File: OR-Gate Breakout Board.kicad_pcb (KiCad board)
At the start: 2 copper layers, 5.5 x 5.4 mm, 8 parts, among them U5 74LVC1G332GW,125

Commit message: Updated design to be a little more usable. Still need to consider resistors and stuff. Do not use this version. WIP
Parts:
- added ?: , , F.Cu at (155.2, 97.8)
- moved ? 8.84 mm to (142.2, 99.1)
- moved ? 8.67 mm to (142.2, 92.7)
- moved ? 8.61 mm to (142.2, 95.8)
- moved C1 5.19 mm to (147.9, 99.1)
- moved U5 5.08 mm to (147.9, 95.5)
- moved ? 2.44 mm to (154.4, 99.3)
- moved ? 1.96 mm to (153.7, 92.7)
- moved ? 1.52 mm to (153.7, 95.8)
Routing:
- net GND: track 4.08 -> 8.85 mm
- net VCC: track 4.46 -> 8.88 mm
- net OUT: track 1.25 -> 5.61 mm
- net B: track 1.17 -> 5.35 mm
- net C: track 1.25 -> 5.10 mm
- net A: track 1.23 -> 5.02 mm
- removed copper zone on B.Cu, net GND
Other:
- board size 5.5 x 5.4 mm -> 17 x 9.1 mm
- board text added: "A"
- board text added: "B"
- board text added: "C"
- board text added: "GND"
- board text added: "OUT"
- board text added: "VCC"

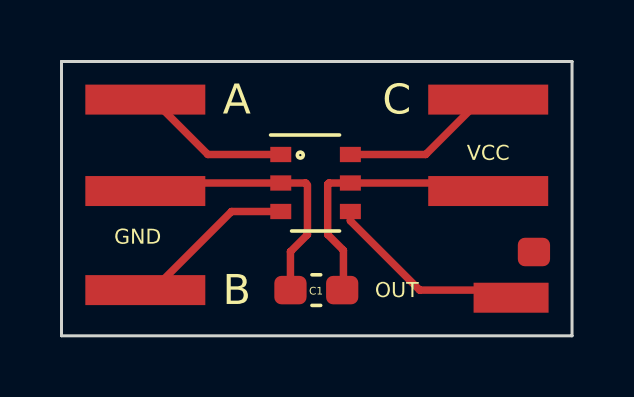
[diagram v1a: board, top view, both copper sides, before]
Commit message: Alpha Prototype for OR Gate Breakout.
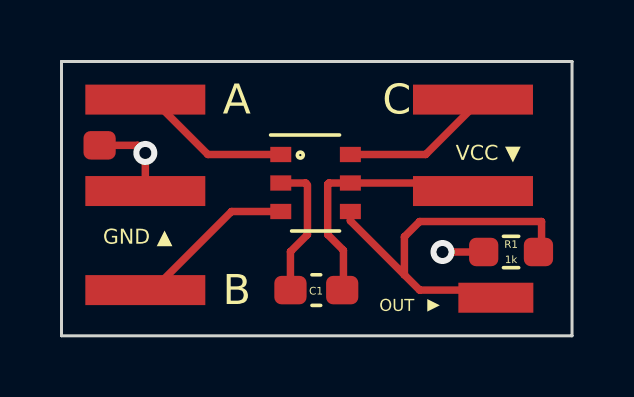
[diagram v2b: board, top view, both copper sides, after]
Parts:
- added 1k: 1k, Resistor_SMD:R_0603_1608Metric_Pad0.98x0.95mm_HandSolder, F.Cu at (154.4, 97.8)
- moved ? 14.9 mm to (140.7, 94.2)
- moved ? 0.51 mm to (153.2, 95.8)
- moved ? 0.51 mm to (153.9, 99.3)
- moved ? 0.51 mm to (153.2, 92.7)
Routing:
- net OUT: track 5.61 -> 12.7 mm
- net GND: track 8.85 -> 9.13 mm, vias 0 -> 2
- added copper zone on B.Cu, net GND
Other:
- board text added: "GND ▲"
- board text added: "R1"
- board text added: "VCC ▼"
- board text added: "▲"
- board text removed: "GND"
- board text removed: "VCC"
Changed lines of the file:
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@@
   )
   (footprint "" (layer "F.Cu")
-    (at 153.67 95.758)
+    (at 153.162 95.758)
     (fp_text reference "" (at 0 0) (layer "F.SilkS")
       (effects (font (size 1.27 1.27) (thickness 0.15)))
@@
   )
   (footprint "" (layer "F.Cu")
-    (at 154.432 99.314)
+    (at 153.924 99.314)
     (fp_text reference "" (at 0 0) (layer "F.SilkS")
       (effects (font (size 1.27 1.27) (thickness 0.15)))
@@
       (net 2 "GND"))
   )
-  (footprint "" (layer "F.Cu")
-    (at 155.194 97.79)
-    (fp_text reference "" (at 0 0) (layer "F.SilkS")
-      (effects (font (size 1.27 1.27) (thickness 0.15)))
-    )
-    (fp_text value "" (at 0 0) (layer "F.SilkS")
-      (effects (font (size 1.27 1.27) (thickness 0.15)))
-    )
-    (pad "4" smd roundrect locked (at 0 0) (size 1.075 0.95) (layers "F.Cu" "F.Paste" "F.Mask") (roundrect_rratio 0.25)
+  (footprint "Resistor_SMD:R_0603_1608Metric_Pad0.98x0.95mm_HandSolder" (layer "F.Cu")
+    (at 154.432 97.79)
+    (descr "Resistor SMD 0603 (1608 Metric), square (rectangular) end terminal, IPC_7351 nominal with elongated pad for handsoldering. (Body size source: IPC-SM-782 page 72, https://www.pcb-3d.com/wordpress/wp-content/uploads/ipc-sm-782a_amendment_1_and_2.pdf), generated with kicad-footprint-generator")
+    (tags "resistor handsolder")
+    (attr smd)
+    (fp_text reference "1k" (at 0 0.254) (layer "F.SilkS")
+      (effects (font (size 0.25 0.25) (thickness 0.0625)))
+    )
+    (fp_text value "1k" (at 0 1.43) (layer "F.Fab")
+      (effects (font (size 1 1) (thickness 0.15)))
+    )
+    (fp_text user "${REFERENCE}" (at 0 0) (layer "F.Fab")
+      (effects (font (size 0.4 0.4) (thickness 0.06)))
+    )
+    (fp_line (start -0.254724 0.5225) (end 0.254724 0.5225) (layer "F.SilkS") (width 0.12))
+    (fp_line (start -0.254724 -0.5225) (end 0.254724 -0.5225) (layer "F.SilkS") (width 0.12))
+    (fp_line (start -1.65 -0.73) (end 1.65 -0.73) (layer "F.CrtYd") (width 0.05))
+    (fp_line (start 1.65 -0.73) (end 1.65 0.73) (layer "F.CrtYd") (width 0.05))
+    (fp_line (start -1.65 0.73) (end -1.65 -0.73) (layer "F.CrtYd") (width 0.05))
+    (fp_line (start 1.65 0.73) (end -1.65 0.73) (layer "F.CrtYd") (width 0.05))
+    (fp_line (start 0.8 -0.4125) (end 0.8 0.4125) (layer "F.Fab") (width 0.1))
+    (fp_line (start 0.8 0.4125) (end -0.8 0.4125) (layer "F.Fab") (width 0.1))
+    (fp_line (start -0.8 -0.4125) (end 0.8 -0.4125) (layer "F.Fab") (width 0.1))
+    (fp_line (start -0.8 0.4125) (end -0.8 -0.4125) (layer "F.Fab") (width 0.1))
+    (pad "7" smd roundrect (at -0.9125 0) (size 0.975 0.95) (layers "F.Cu" "F.Paste" "F.Mask") (roundrect_rratio 0.25)
+      (net 2 "GND"))
+    (pad "8" smd roundrect (at 0.9125 0) (size 0.975 0.95) (layers "F.Cu" "F.Paste" "F.Mask") (roundrect_rratio 0.25)
       (net 4 "OUT"))
+    (model "${KICAD6_3DMODEL_DIR}/Resistor_SMD.3dshapes/R_0603_1608Metric.wrl"
+      (offset (xyz 0 0 0))
+      (scale (xyz 1 1 1))
+      (rotate (xyz 0 0 0))
+    )
   )
   (footprint "" (layer "F.Cu")
@@
   )
   (footprint "" (layer "F.Cu")
-    (at 153.67 92.71)
+    (at 140.716 94.234)
+    (fp_text reference "" (at 0 0) (layer "F.SilkS")
+      (effects (font (size 1.27 1.27) (thickness 0.15)))
+    )
+    (fp_text value "" (at 0 0) (layer "F.SilkS")
+      (effects (font (size 1.27 1.27) (thickness 0.15)))
+    )
+    (pad "1" smd roundrect (at 0 0) (size 1.075 0.95) (layers "F.Cu" "F.Paste" "F.Mask") (roundrect_rratio 0.25)
+      (net 2 "GND"))
+  )
+  (footprint "" (layer "F.Cu")
+    (at 153.162 92.71)
     (fp_text reference "" (at 0 0) (layer "F.SilkS")
       (effects (font (size 1.27 1.27) (thickness 0.15)))
@@
   )
   (gr_rect (start 139.446 91.44) (end 156.464 100.584) (layer "Edge.Cuts") (width 0.1) (fill none))
-  (gr_text "GND" (at 141.986 97.282) (layer "F.SilkS")
+  (gr_text "GND ▲" (at 141.986 97.282) (layer "F.SilkS")
     (effects (font (size 0.5 0.5) (thickness 0.125)))
   )
@@
     (effects (font (size 1 1) (thickness 0.15)))
   )
-  (gr_text "VCC" (at 153.67 94.488) (layer "F.SilkS")
+  (gr_text "VCC ▼" (at 153.67 94.488) (layer "F.SilkS")
     (effects (font (size 0.5 0.5) (thickness 0.125)))
+  )
+  (gr_text "▲" (at 151.892 99.568 -90) (layer "F.SilkS")
+    (effects (font (size 0.4 0.4) (thickness 0.1)))
+  )
+  (gr_text "R1" (at 154.432 97.536) (layer "F.SilkS")
+    (effects (font (size 0.25 0.25) (thickness 0.0625)))
   )
   (gr_text "B" (at 145.288 99.06) (layer "F.SilkS")
     (effects (font (size 1 1) (thickness 0.15)))
   )
-  (gr_text "OUT" (at 150.622 99.06) (layer "F.SilkS")
-    (effects (font (size 0.5 0.5) (thickness 0.125)))
+  (gr_text "OUT" (at 150.622 99.568) (layer "F.SilkS")
+    (effects (font (size 0.4 0.4) (thickness 0.1)))
   )
   (gr_text "C" (at 150.622 92.71) (layer "F.SilkS")
@@
   (segment (start 142.494 92.71) (end 144.324 94.54) (width 0.25) (layer "F.Cu") (net 1))
   (segment (start 144.324 94.54) (end 146.755 94.54) (width 0.25) (layer "F.Cu") (net 1))
+  (segment (start 152.146 97.79) (end 153.5195 97.79) (width 0.25) (layer "F.Cu") (net 2))
   (segment (start 146.91 95.49) (end 146.89 95.51) (width 0.25) (layer "F.Cu") (net 2))
   (segment (start 147.0775 97.7785) (end 147.0775 99.06) (width 0.25) (layer "F.Cu") (net 2))
   (segment (start 147.645 95.55) (end 147.645 97.211) (width 0.25) (layer "F.Cu") (net 2))
   (segment (start 147.585 95.49) (end 146.91 95.49) (width 0.25) (layer "F.Cu") (net 2))
+  (segment (start 140.716 94.234) (end 141.986 94.234) (width 0.25) (layer "F.Cu") (net 2))
+  (segment (start 141.986 94.234) (end 142.24 94.488) (width 0.25) (layer "F.Cu") (net 2))
   (segment (start 147.605 95.51) (end 147.585 95.49) (width 0.25) (layer "F.Cu") (net 2))
   (segment (start 142.494 95.758) (end 142.762 95.49) (width 0.25) (layer "F.Cu") (net 2))
   (segment (start 147.645 97.211) (end 147.0775 97.7785) (width 0.25) (layer "F.Cu") (net 2))
-  (segment (start 142.762 95.49) (end 146.755 95.49) (width 0.25) (layer "F.Cu") (net 2))
+  (segment (start 142.24 95.758) (end 142.24 94.488) (width 0.25) (layer "F.Cu") (net 2))
+  (via (at 142.24 94.488) (size 0.8) (drill 0.4) (layers "F.Cu" "B.Cu") (free) (net 2))
+  (via (at 152.146 97.79) (size 0.8) (drill 0.4) (layers "F.Cu" "B.Cu") (net 2))
   (segment (start 145.114 96.44) (end 146.755 96.44) (width 0.25) (layer "F.Cu") (net 3))
   (segment (start 142.494 99.06) (end 145.114 96.44) (width 0.25) (layer "F.Cu") (net 3))
+  (segment (start 150.876 98.552) (end 150.876 97.282) (width 0.25) (layer "F.Cu") (net 4))
+  (segment (start 150.876 98.552) (end 151.384 99.06) (width 0.25) (layer "F.Cu") (net 4))
+  (segment (start 150.876 97.282) (end 151.384 96.774) (width 0.25) (layer "F.Cu") (net 4))
+  (segment (start 155.448 96.774) (end 155.448 97.6865) (width 0.25) (layer "F.Cu") (net 4))
+  (segment (start 155.448 97.6865) (end 155.3445 97.79) (width 0.25) (layer "F.Cu") (net 4))
+  (segment (start 151.384 96.774) (end 155.448 96.774) (width 0.25) (layer "F.Cu") (net 4))
   (segment (start 151.384 99.06) (end 153.416 99.06) (width 0.25) (layer "F.Cu") (net 4))
-  (segment (start 149.075 96.751) (end 151.384 99.06) (width 0.25) (layer "F.Cu") (net 4))
+  (segment (start 149.075 96.751) (end 150.876 98.552) (width 0.25) (layer "F.Cu") (net 4))
   (segment (start 149.075 96.44) (end 149.075 96.751) (width 0.25) (layer "F.Cu") (net 4))
   (segment (start 148.8025 99.06) (end 148.844 99.0185) (width 0.25) (layer "F.Cu") (net 5))
@@
   (segment (start 153.416 92.71) (end 151.586 94.54) (width 0.25) (layer "F.Cu") (net 6))
   (segment (start 151.586 94.54) (end 149.075 94.54) (width 0.25) (layer "F.Cu") (net 6))
+  (zone (net 2) (net_name "GND") (layer "B.Cu") (hatch edge 0.508)
+    (connect_pads (clearance 0.508))
+    (min_thickness 0.254) (filled_areas_thickness no)
+    (fill yes (thermal_gap 0.508) (thermal_bridge_width 0.508))
+    (polygon
+      (pts
+        (xy 156.464 100.584)
+        (xy 139.446 100.584)
+        (xy 139.446 91.44)
+        (xy 156.464 91.44)
+      )
+    )
+  )
 )
